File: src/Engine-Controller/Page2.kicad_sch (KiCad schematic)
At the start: 25 parts, among them P2 Solid Prop Cont, P4 Micro_SD_Card, P5 USB, P6 140-504-415-000, Q1 QS5U17TR, U4 SST25VF040B-50-4I-S2AE-T, U5 CP2102-GMR(QFN28)

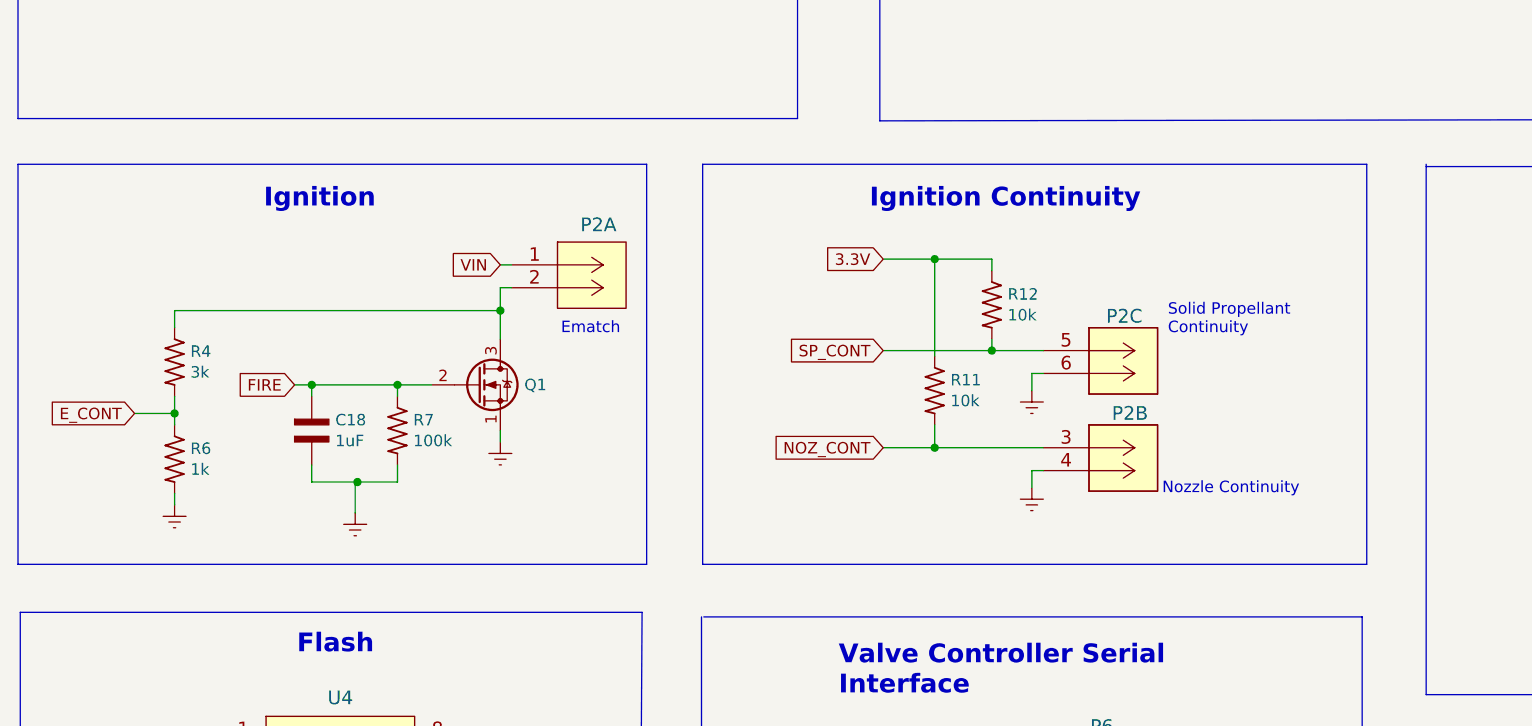
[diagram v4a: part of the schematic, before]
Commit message: corrected comparator symbol pin numbers
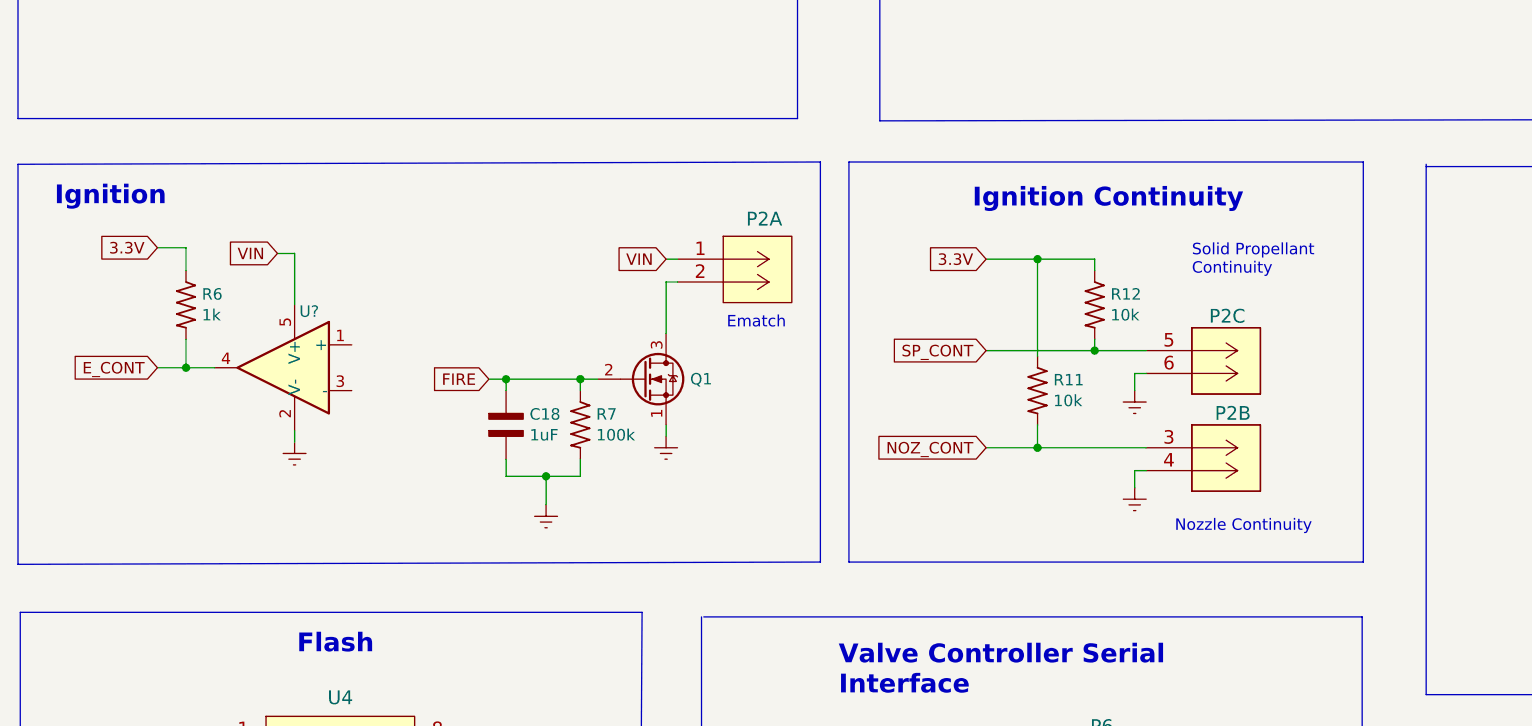
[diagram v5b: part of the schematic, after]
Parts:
- removed R4: 3k, Engine-Controller:RES_0603, symbol Engine-Controller:RES_0603
- added U?: (no value), symbol Engine-Controller:TS391IYLT
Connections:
- net 3.3V: now also R6.1
- net E_CONT: now also R6.2, U?.4; no longer R6.1
- net Earth: now also U?.2 (V-); no longer R6.2
- net VIN: now also U?.5 (V+)
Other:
- moved on the sheet: C18, P2A, P2B, P2C, Q1, R11, R12, R6, R7

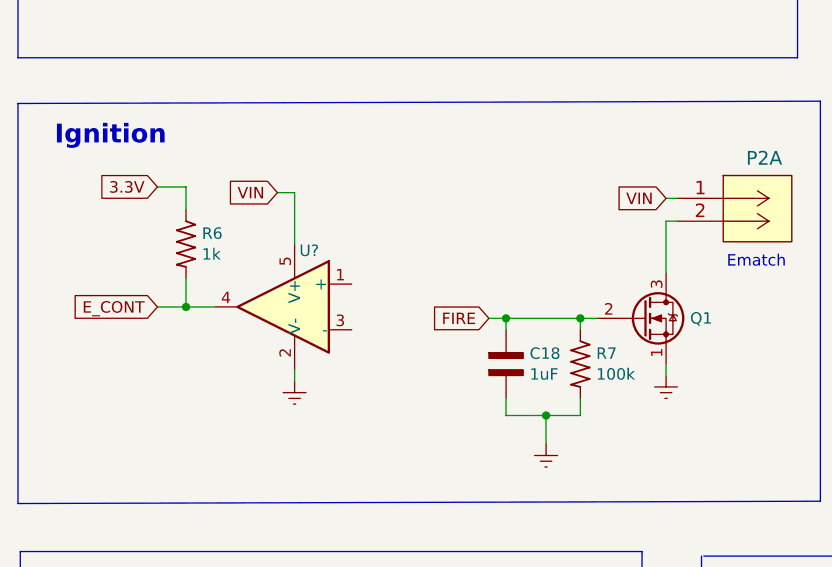
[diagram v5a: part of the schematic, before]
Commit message: added comparator to rev 4.0 schematic
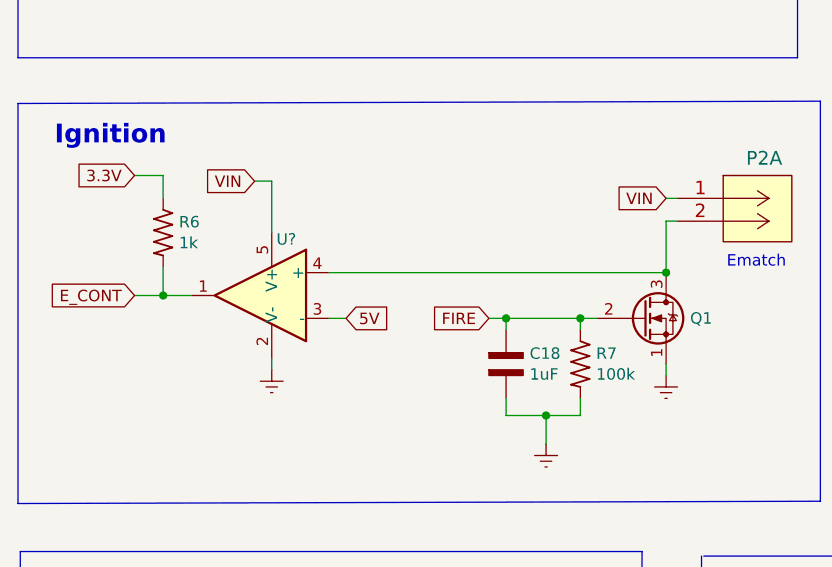
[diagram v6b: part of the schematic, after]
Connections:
- net 5V: now also U?.3 (-)
- net E_CONT: now also U?.1; no longer U?.4
- net at P2.2 (6), Q1.3 (D): now also U?.4 (+)
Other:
- moved on the sheet: R6, U?
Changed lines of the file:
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@@
   (junction (at 240.665 78.74) (diameter 0) (color 0 0 0 0)
   )
-  (junction (at 38.735 124.46) (diameter 0) (color 0 0 0 0)
+  (junction (at 36.195 123.19) (diameter 0) (color 0 0 0 0)
   )
   (junction (at 144.272 66.04) (diameter 0) (color 0 0 0 0)
@@
   )
   (junction (at 78.74 136.525) (diameter 0) (color 0 0 0 0)
+  )
+  (junction (at 92.075 120.65) (diameter 0) (color 0 0 0 0)
   )
   (no_connect (at 248.285 74.93))
@@
     (stroke (width 0) (type default) (color 0 0 0 0))
   )
-  (wire (pts (xy 38.735 111.125) (xy 38.735 113.665))
+  (wire (pts (xy 36.195 109.855) (xy 36.195 112.395))
     (stroke (width 0) (type default) (color 0 0 0 0))
   )
@@
     (stroke (width 0) (type default) (color 0 0 0 0))
   )
+  (wire (pts (xy 54.61 125.73) (xy 56.515 125.73))
+    (stroke (width 0) (type default) (color 0 0 0 0))
+  )
   (wire (pts (xy 50.8 57.15) (xy 49.53 57.15))
     (stroke (width 0) (type default) (color 0 0 0 0))
@@
     (stroke (width 0) (type default) (color 0 0 0 0))
   )
-  (wire (pts (xy 50.8 131.445) (xy 50.8 132.715))
+  (wire (pts (xy 48.26 130.175) (xy 48.26 131.445))
     (stroke (width 0) (type default) (color 0 0 0 0))
   )
@@
     (stroke (width 0) (type default) (color 0 0 0 0))
   )
-  (wire (pts (xy 35.56 111.125) (xy 38.735 111.125))
+  (wire (pts (xy 33.02 109.855) (xy 36.195 109.855))
     (stroke (width 0) (type default) (color 0 0 0 0))
   )
@@
     (stroke (width 0) (type default) (color 0 0 0 0))
   )
-  (wire (pts (xy 48.895 111.76) (xy 50.8 111.76))
+  (wire (pts (xy 46.355 110.49) (xy 48.26 110.49))
     (stroke (width 0) (type default) (color 0 0 0 0))
   )
@@
     (stroke (width 0) (type default) (color 0 0 0 0))
   )
-  (wire (pts (xy 38.735 124.46) (xy 41.91 124.46))
+  (wire (pts (xy 36.195 123.19) (xy 39.37 123.19))
     (stroke (width 0) (type default) (color 0 0 0 0))
   )
@@
     (stroke (width 0) (type default) (color 0 0 0 0))
   )
+  (wire (pts (xy 54.61 120.65) (xy 92.075 120.65))
+    (stroke (width 0) (type default) (color 0 0 0 0))
+  )
   (wire (pts (xy 85.09 73.914) (xy 85.09 75.184))
     (stroke (width 0) (type default) (color 0 0 0 0))
@@
     (stroke (width 0) (type default) (color 0 0 0 0))
   )
-  (wire (pts (xy 35.56 124.46) (xy 38.735 124.46))
+  (wire (pts (xy 33.02 123.19) (xy 36.195 123.19))
     (stroke (width 0) (type default) (color 0 0 0 0))
   )
@@
     (stroke (width 0) (type default) (color 0 0 0 0))
   )
-  (wire (pts (xy 38.735 121.285) (xy 38.735 124.46))
+  (wire (pts (xy 36.195 120.015) (xy 36.195 123.19))
     (stroke (width 0) (type default) (color 0 0 0 0))
   )
@@
     (stroke (width 0) (type default) (color 0 0 0 0))
   )
-  (wire (pts (xy 50.8 111.76) (xy 50.8 117.475))
+  (wire (pts (xy 48.26 110.49) (xy 48.26 116.205))
     (stroke (width 0) (type default) (color 0 0 0 0))
   )
@@
     )
   )
-  (global_label "3.3V" (shape input) (at 35.56 111.125 180) (fields_autoplaced)
-    (effects (font (size 1.27 1.27)) (justify right))
-    (property "Intersheet References" "${INTERSHEET_REFS}" (id 0) (at -85.09 34.925 0)
+  (global_label "3.3V" (shape input) (at 33.02 109.855 180) (fields_autoplaced)
+    (effects (font (size 1.27 1.27)) (justify right))
+    (property "Intersheet References" "${INTERSHEET_REFS}" (id 0) (at -87.63 33.655 0)
       (effects (font (size 1.27 1.27)) hide)
     )
@@
     )
   )
+  (global_label "5V" (shape input) (at 56.515 125.73 0) (fields_autoplaced)
+    (effects (font (size 1.27 1.27)) (justify left))
+    (property "Intersheet References" "${INTERSHEET_REFS}" (id 0) (at 61.1373 125.8094 0)
+      (effects (font (size 1.27 1.27)) (justify left) hide)
+    )
+  )
   (global_label "~{USB_SUSPEND}" (shape input) (at 227.076 78.74 180) (fields_autoplaced)
     (effects (font (size 1.27 1.27)) (justify right))
@@
     )
   )
-  (global_label "E_CONT" (shape input) (at 35.56 124.46 180) (fields_autoplaced)
-    (effects (font (size 1.27 1.27)) (justify right))
-    (property "Intersheet References" "${INTERSHEET_REFS}" (id 0) (at -45.72 24.765 0)
+  (global_label "E_CONT" (shape input) (at 33.02 123.19 180) (fields_autoplaced)
+    (effects (font (size 1.27 1.27)) (justify right))
+    (property "Intersheet References" "${INTERSHEET_REFS}" (id 0) (at -48.26 23.495 0)
       (effects (font (size 1.27 1.27)) hide)
     )
@@
     )
   )
-  (global_label "VIN" (shape input) (at 48.895 111.76 180) (fields_autoplaced)
-    (effects (font (size 1.27 1.27)) (justify right))
-    (property "Intersheet References" "${INTERSHEET_REFS}" (id 0) (at -29.845 236.22 0)
+  (global_label "VIN" (shape input) (at 46.355 110.49 180) (fields_autoplaced)
+    (effects (font (size 1.27 1.27)) (justify right))
+    (property "Intersheet References" "${INTERSHEET_REFS}" (id 0) (at -32.385 234.95 0)
       (effects (font (size 1.27 1.27)) hide)
     )
@@
     (pin "2")
   )
-  (symbol (lib_id "Engine-Controller:RES_0603") (at 38.735 117.475 270) (unit 1)
-    (in_bom yes) (on_board yes)
-    (property "Reference" "R6" (id 0) (at 40.4876 116.3066 90)
+  (symbol (lib_id "Engine-Controller:RES_0603") (at 36.195 116.205 270) (unit 1)
+    (in_bom yes) (on_board yes)
+    (property "Reference" "R6" (id 0) (at 37.9476 115.0366 90)
       (effects (font (size 1.27 1.27)) (justify left))
     )
-    (property "Value" "1k" (id 1) (at 40.4876 118.618 90)
+    (property "Value" "1k" (id 1) (at 37.9476 117.348 90)
       (effects (font (size 1.27 1.27)) (justify left))
     )
-    (property "Footprint" "Engine-Controller:RES_0603" (id 2) (at 26.035 118.745 0)
+    (property "Footprint" "Engine-Controller:RES_0603" (id 2) (at 23.495 117.475 0)
       (effects (font (size 1.27 1.27)) (justify left bottom) hide)
     )
-    (property "Datasheet" "" (id 3) (at 38.735 117.475 0)
+    (property "Datasheet" "" (id 3) (at 36.195 116.205 0)
       (effects (font (size 1.27 1.27)) (justify left bottom) hide)
     )
@@
     (pin "2")
   )
-  (symbol (lib_id "Engine-Controller:Earth") (at 50.8 132.715 0) (unit 1)
-    (in_bom yes) (on_board yes)
-    (property "Reference" "#PWR?" (id 0) (at 50.8 139.065 0)
-      (effects (font (size 1.27 1.27)) hide)
-    )
-    (property "Value" "Earth" (id 1) (at 50.8 136.525 0)
-      (effects (font (size 1.27 1.27)) hide)
-    )
-    (property "Footprint" "" (id 2) (at 50.8 132.715 0)
-      (effects (font (size 1.27 1.27)) hide)
-    )
-    (property "Datasheet" "" (id 3) (at 50.8 132.715 0)
+  (symbol (lib_id "Engine-Controller:Earth") (at 48.26 131.445 0) (unit 1)
+    (in_bom yes) (on_board yes)
+    (property "Reference" "#PWR?" (id 0) (at 48.26 137.795 0)
+      (effects (font (size 1.27 1.27)) hide)
+    )
+    (property "Value" "Earth" (id 1) (at 48.26 135.255 0)
+      (effects (font (size 1.27 1.27)) hide)
+    )
+    (property "Footprint" "" (id 2) (at 48.26 131.445 0)
+      (effects (font (size 1.27 1.27)) hide)
+    )
+    (property "Datasheet" "" (id 3) (at 48.26 131.445 0)
       (effects (font (size 1.27 1.27)) hide)
     )
@@
     (pin "6")
   )
-  (symbol (lib_id "Engine-Controller:TS391IYLT") (at 49.53 124.46 0) (mirror y) (unit 1)
+  (symbol (lib_id "Engine-Controller:TS391IYLT") (at 46.99 123.19 0) (mirror y) (unit 1)
     (in_bom yes) (on_board yes) (fields_autoplaced)
-    (property "Reference" "U?" (id 0) (at 51.3206 118.2172 0)
+    (property "Reference" "U?" (id 0) (at 48.7806 116.9472 0)
       (effects (font (size 1.27 1.27)) (justify right))
     )
-    (property "Value" "" (id 1) (at 45.72 129.54 0)
-      (effects (font (size 1.27 1.27)) hide)
-    )
-    (property "Footprint" "" (id 2) (at 49.53 121.92 0)
-      (effects (font (size 1.27 1.27)) hide)
-    )
-    (property "Datasheet" "" (id 3) (at 49.53 119.38 0)
-      (effects (font (size 1.27 1.27)) hide)
-    )
+    (property "Value" "" (id 1) (at 43.18 128.27 0)
+      (effects (font (size 1.27 1.27)) hide)
+    )
+    (property "Footprint" "" (id 2) (at 46.99 120.65 0)
+      (effects (font (size 1.27 1.27)) hide)
+    )
+    (property "Datasheet" "" (id 3) (at 46.99 118.11 0)
+      (effects (font (size 1.27 1.27)) hide)
+    )

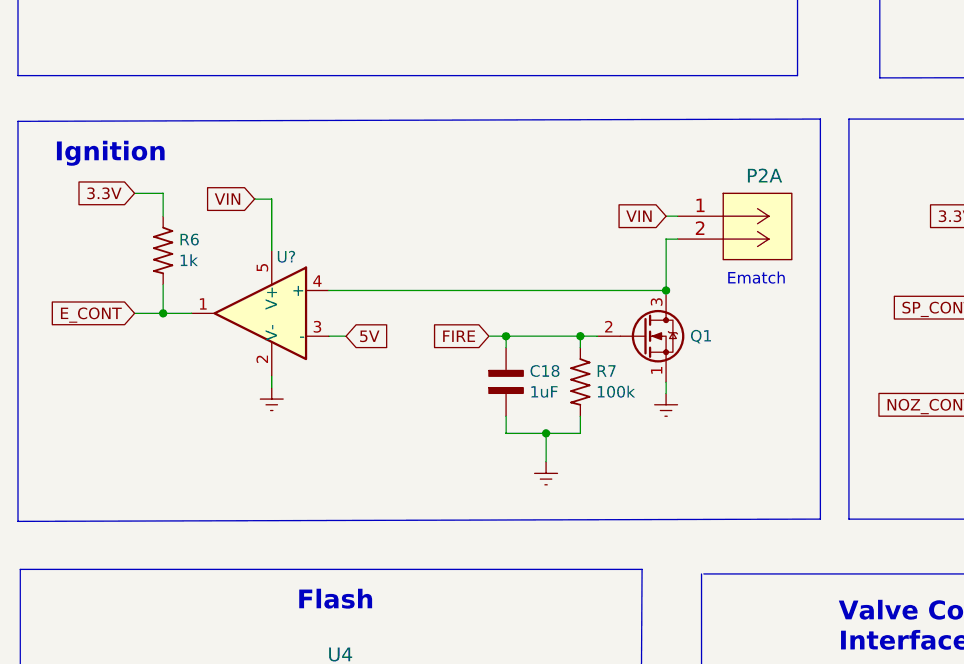
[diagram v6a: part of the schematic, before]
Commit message: fixed pinout of MOSFET symbol
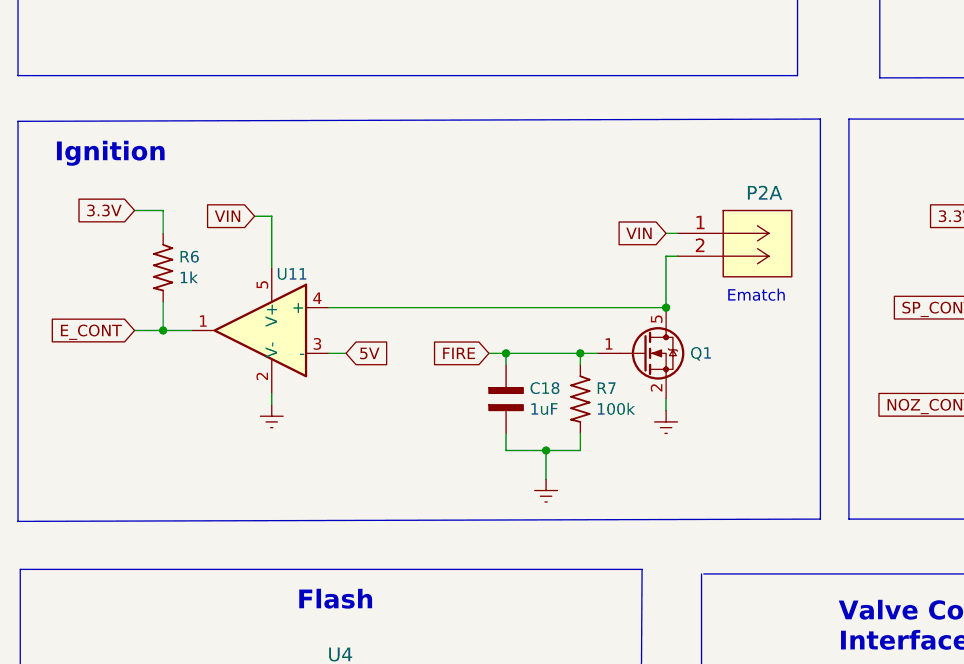
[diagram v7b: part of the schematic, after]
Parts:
- Q1: value QS5U17TR -> (none); footprint Engine-Controller:QS5U17TR -> Package_TO_SOT_THT:TO-92_Inline
- U11: renamed from U?; value (none) -> TS391IYLT
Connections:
- net Earth: now also Q1.2 (S); no longer Q1.1 (S)
- net FIRE: now also Q1.1 (G); no longer Q1.2 (G)
- net at P2.2 (6), U11.4 (+): now also Q1.5 (D); no longer Q1.3 (D)
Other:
- moved on the sheet: C18, P2A, Q1, R6, R7, U11
